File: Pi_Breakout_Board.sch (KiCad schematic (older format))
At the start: 74 parts, among them J1 Raspberry_Pi_2_3, J2 Conn_02x04_Odd_Even heater he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, J3 Conn_02x08_Odd_Even thermisto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, J4 Screw_Terminal_01x02, J5 Conn_01x08_Male, J6 Conn_01x08_Male, J7 Conn_01x05_Male uart breakout, Q1 Q_NMOS_GDSD, Q2 Q_NMOS_GDSD, Q3 Q_NMOS_GDSD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

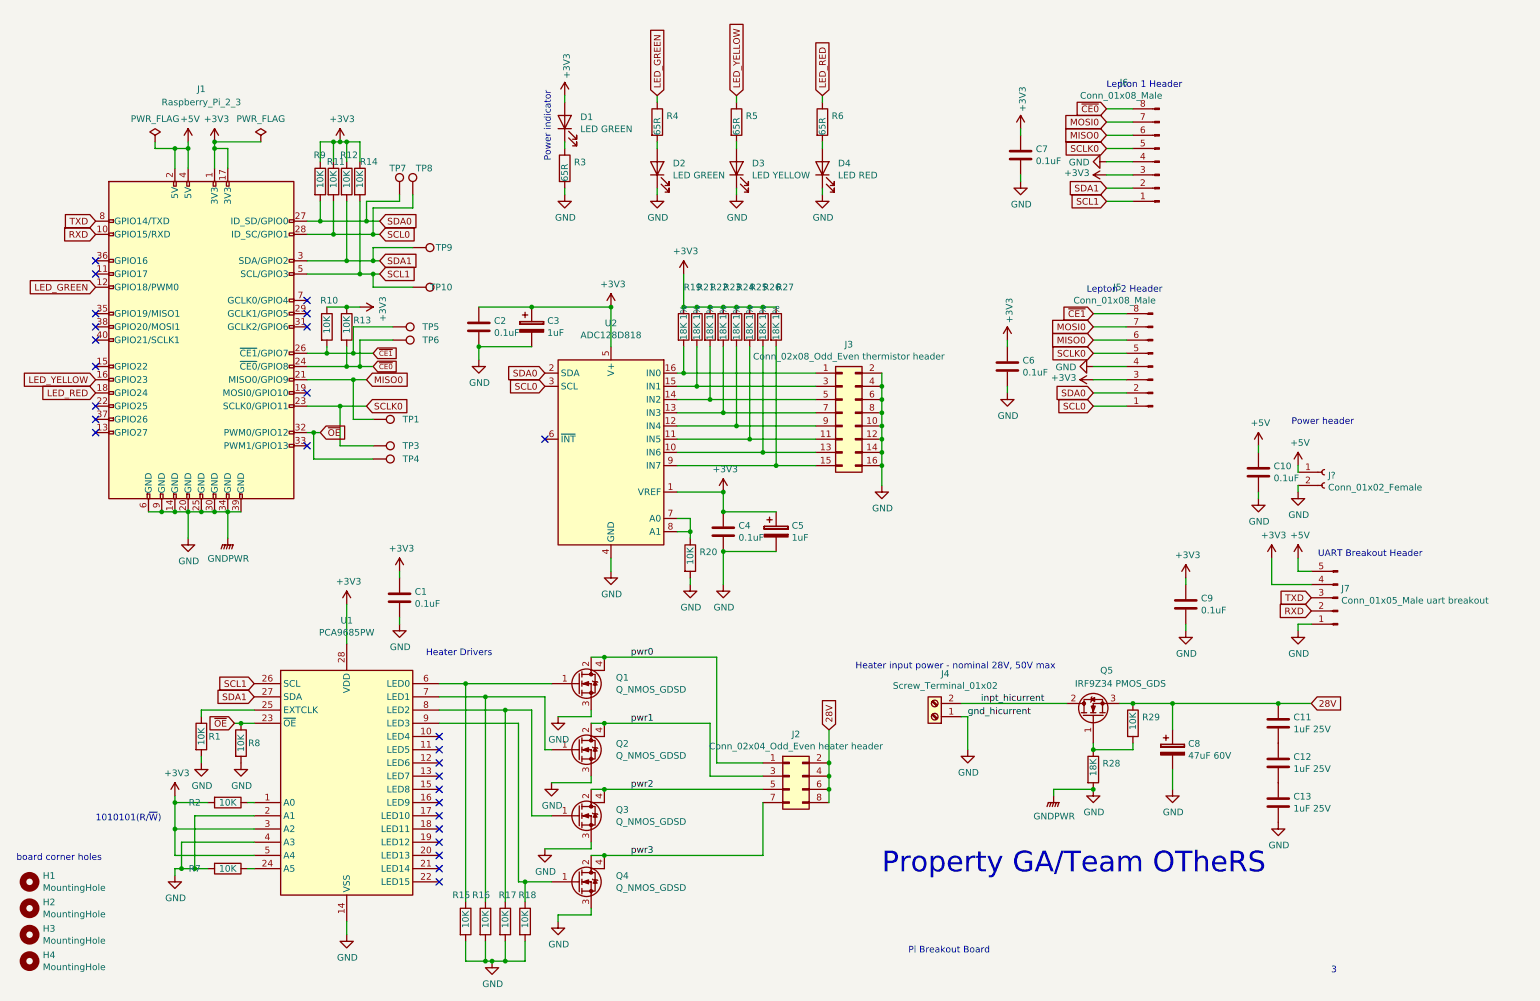
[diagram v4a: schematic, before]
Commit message: Remove power lines from UART breakout header
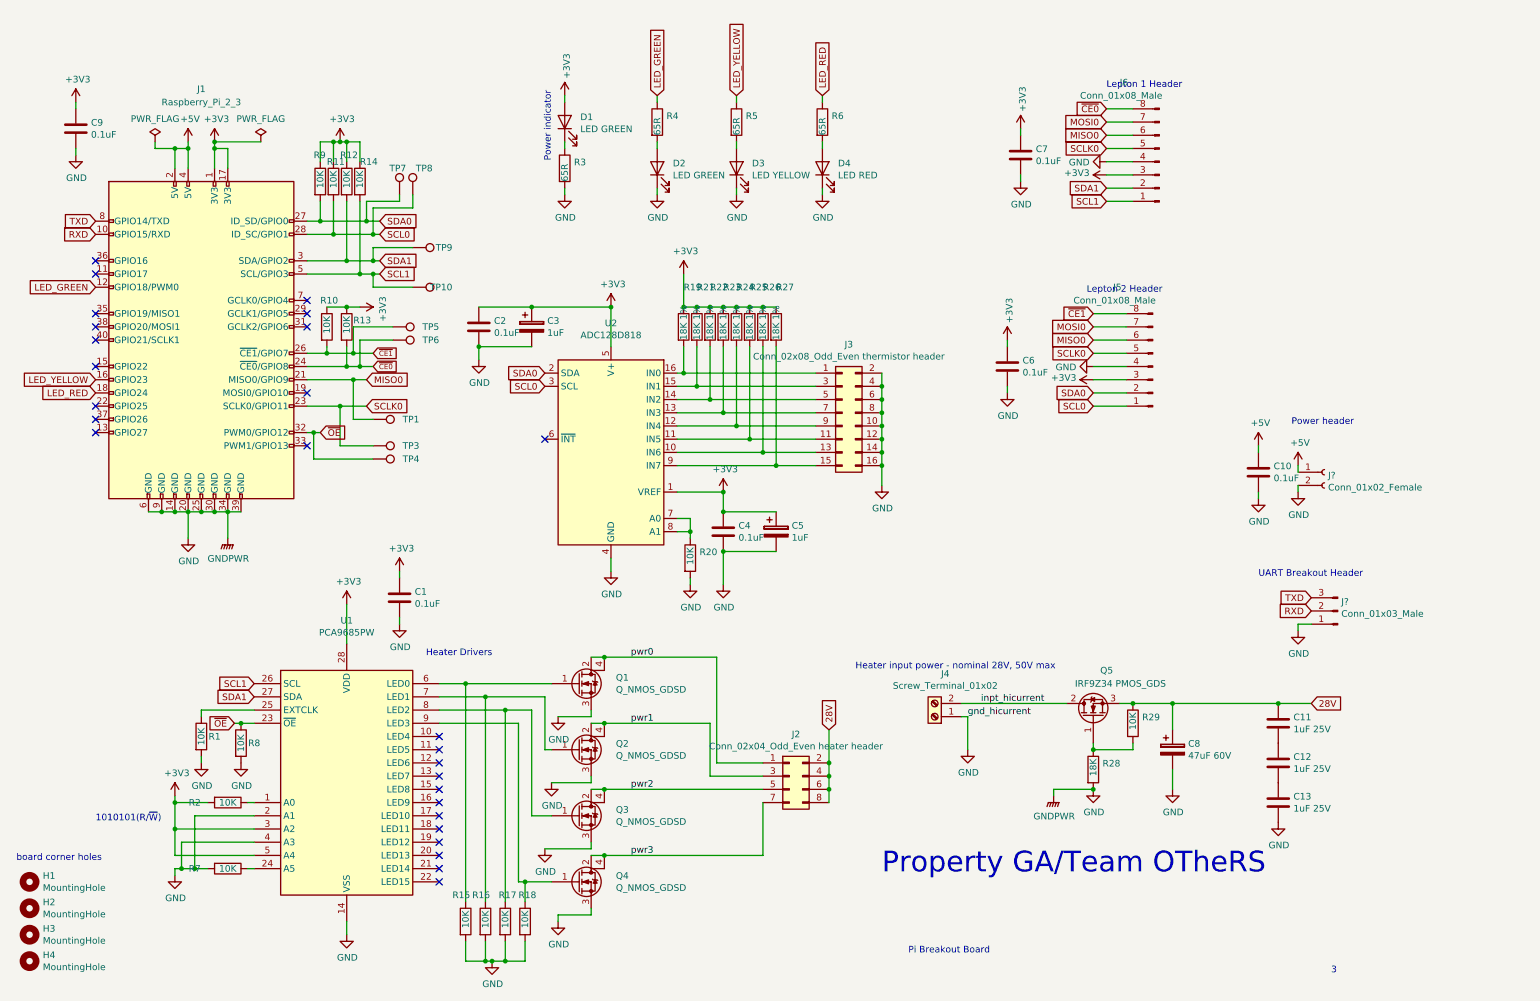
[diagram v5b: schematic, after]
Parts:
- removed J7: Conn_01x05_Male uart breakout, Connector_PinHeader_2.54mm:PinHeader_1x05_P2.54mm_Vertical, symbol Connector:Conn_01x05_Male
- added J?: Conn_01x03_Male, symbol Connector:Conn_01x03_Male
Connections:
- net GND: now also J?.1 (Pin_1)
- net RXD: now also J?.2 (Pin_2)
- net TXD: now also J?.3 (Pin_3)
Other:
- moved on the sheet: C9
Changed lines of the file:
@@
 Text GLabel 10450 4900 0    50   Input ~ 0
 RXD
-Text Notes 10500 4500 0    50   ~ 0
+Text Notes 10050 4650 0    50   ~ 0
 UART Breakout Header
 Text Notes 7000 5350 0    50   ~ 0
@@
 L Device:C C9
 U 1 1 5C58CD61
-P 9500 4850
-F 0 "C9" H 9615 4896 50  0000 L CNN
-F 1 "0.1uF" H 9615 4805 50  0000 L CNN
-F 2 "Capacitor_SMD:C_1210_3225Metric_Pad1.42x2.65mm_HandSolder" H 9538 4700 50  0001 C CNN
-F 3 "~" H 9500 4850 50  0001 C CNN
-	1    9500 4850
-	1    0    0    -1
-$EndComp
-Wire Wire Line
-	9500 4650 9500 4700
+P 1100 1250
+F 0 "C9" H 1215 1296 50  0000 L CNN
+F 1 "0.1uF" H 1215 1205 50  0000 L CNN
+F 2 "Capacitor_SMD:C_1210_3225Metric_Pad1.42x2.65mm_HandSolder" H 1138 1100 50  0001 C CNN
+F 3 "~" H 1100 1250 50  0001 C CNN
+	1    1100 1250
+	1    0    0    -1
+$EndComp
+Wire Wire Line
+	1100 1050 1100 1100
 $Comp
 L power:GND #PWR041
 U 1 1 5C58CD69
-P 9500 5050
-F 0 "#PWR041" H 9500 4800 50  0001 C CNN
-F 1 "GND" H 9505 4877 50  0000 C CNN
-F 2 "" H 9500 5050 50  0001 C CNN
-F 3 "" H 9500 5050 50  0001 C CNN
-	1    9500 5050
-	1    0    0    -1
-$EndComp
-Wire Wire Line
-	9500 5000 9500 5050
+P 1100 1450
+F 0 "#PWR041" H 1100 1200 50  0001 C CNN
+F 1 "GND" H 1105 1277 50  0000 C CNN
+F 2 "" H 1100 1450 50  0001 C CNN
+F 3 "" H 1100 1450 50  0001 C CNN
+	1    1100 1450
+	1    0    0    -1
+$EndComp
+Wire Wire Line
+	1100 1400 1100 1450
 $Comp
 L power:+3V3 #PWR040
 U 1 1 5C59BE3C
-P 9500 4650
-F 0 "#PWR040" H 9500 4500 50  0001 C CNN
-F 1 "+3V3" H 9515 4823 50  0000 C CNN
-F 2 "" H 9500 4650 50  0001 C CNN
-F 3 "" H 9500 4650 50  0001 C CNN
-	1    9500 4650
-	1    0    0    -1
-$EndComp
-$Comp
-L Connector:Conn_01x05_Male J7
-U 1 1 5C59C913
-P 10650 4800
-F 0 "J7" H 10623 4730 50  0000 R CNN
-F 1 "Conn_01x05_Male uart breakout" H 10623 4821 50  0000 R CNN
-F 2 "Connector_PinHeader_2.54mm:PinHeader_1x05_P2.54mm_Vertical" H 10650 4800 50  0001 C CNN
-F 3 "~" H 10650 4800 50  0001 C CNN
-	1    10650 4800
-	-1   0    0    1
-$EndComp
-Wire Wire Line
-	10450 4600 10350 4600
-Wire Wire Line
-	10350 4600 10350 4500
-$Comp
-L power:+3V3 #PWR044
-U 1 1 5C5BAA9F
-P 10150 4500
-F 0 "#PWR044" H 10150 4350 50  0001 C CNN
-F 1 "+3V3" H 10165 4673 50  0000 C CNN
-F 2 "" H 10150 4500 50  0001 C CNN
-F 3 "" H 10150 4500 50  0001 C CNN
-	1    10150 4500
-	1    0    0    -1
-$EndComp
-Wire Wire Line
-	10150 4500 10150 4700
-Wire Wire Line
-	10150 4700 10450 4700
+P 1100 1050
+F 0 "#PWR040" H 1100 900 50  0001 C CNN
+F 1 "+3V3" H 1115 1223 50  0000 C CNN
+F 2 "" H 1100 1050 50  0001 C CNN
+F 3 "" H 1100 1050 50  0001 C CNN
+	1    1100 1050
+	1    0    0    -1
+$EndComp
 $Comp
 L Device:R R7
@@
 Power header
 $Comp
-L power:+5V #PWR?
-U 1 1 5C94934F
-P 10350 4500
-F 0 "#PWR?" H 10350 4350 50  0001 C CNN
-F 1 "+5V" H 10365 4673 50  0000 C CNN
-F 2 "" H 10350 4500 50  0001 C CNN
-F 3 "" H 10350 4500 50  0001 C CNN
-	1    10350 4500
-	1    0    0    -1
+L Connector:Conn_01x03_Male J?
+U 1 1 5C9743D8
+P 10650 4900
+F 0 "J?" H 10623 4830 50  0000 R CNN
+F 1 "Conn_01x03_Male" H 10623 4921 50  0000 R CNN
+F 2 "" H 10650 4900 50  0001 C CNN
+F 3 "~" H 10650 4900 50  0001 C CNN
+	1    10650 4900
+	-1   0    0    1
 $EndComp
 $EndSCHEMATC

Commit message: misc routing
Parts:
- J7: renamed from J?; footprint (none) -> Connector_PinSocket_2.54mm:PinSocket_1x02_P2.54mm_Horizontal
- J8: renamed from J?; footprint (none) -> Connector_PinHeader_2.54mm:PinHeader_1x03_P2.54mm_Vertical
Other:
- note added: "Status Indicators"
- moved on the sheet: D2, D4, R4, R6
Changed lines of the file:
@@
 L Device:LED D2
 U 1 1 5C854E19
-P 5500 1550
-F 0 "D2" V 5538 1432 50  0000 R CNN
-F 1 "LED GREEN" V 5447 1432 50  0000 R CNN
-F 2 "LED_SMD:LED_0805_2012Metric_Pad1.15x1.40mm_HandSolder" H 5500 1550 50  0001 C CNN
-F 3 "~" H 5500 1550 50  0001 C CNN
-	1    5500 1550
+P 5750 1550
+F 0 "D2" V 5788 1432 50  0000 R CNN
+F 1 "LED GREEN" H 5650 1400 50  0000 R CNN
+F 2 "LED_SMD:LED_0805_2012Metric_Pad1.15x1.40mm_HandSolder" H 5750 1550 50  0001 C CNN
+F 3 "~" H 5750 1550 50  0001 C CNN
+	1    5750 1550
 	0    -1   -1   0
 $EndComp
@@
 L power:GND #PWR050
 U 1 1 5C854E2D
-P 5500 1750
-F 0 "#PWR050" H 5500 1500 50  0001 C CNN
-F 1 "GND" H 5505 1577 50  0000 C CNN
-F 2 "" H 5500 1750 50  0001 C CNN
-F 3 "" H 5500 1750 50  0001 C CNN
-	1    5500 1750
+P 5750 1750
+F 0 "#PWR050" H 5750 1500 50  0001 C CNN
+F 1 "GND" H 5755 1577 50  0000 C CNN
+F 2 "" H 5750 1750 50  0001 C CNN
+F 3 "" H 5750 1750 50  0001 C CNN
+	1    5750 1750
 	1    0    0    -1
 $EndComp
 Wire Wire Line
-	5500 1000 5500 1050
+	5750 1000 5750 1050
 Wire Wire Line
-	5500 1350 5500 1400
+	5750 1350 5750 1400
 Wire Wire Line
-	5500 1700 5500 1750
+	5750 1700 5750 1750
 $Comp
 L Device:LED D3
@@
 P 6100 1550
 F 0 "D3" V 6138 1433 50  0000 R CNN
-F 1 "LED YELLOW" V 6047 1433 50  0000 R CNN
+F 1 "LED YELLOW" H 6000 1400 50  0000 R CNN
 F 2 "LED_SMD:LED_0805_2012Metric_Pad1.15x1.40mm_HandSolder" H 6100 1550 50  0001 C CNN
 F 3 "~" H 6100 1550 50  0001 C CNN
@@
 L Device:LED D4
 U 1 1 5C87E05E
-P 6750 1550
-F 0 "D4" V 6788 1432 50  0000 R CNN
-F 1 "LED RED" V 6697 1432 50  0000 R CNN
-F 2 "LED_SMD:LED_0805_2012Metric_Pad1.15x1.40mm_HandSolder" H 6750 1550 50  0001 C CNN
-F 3 "~" H 6750 1550 50  0001 C CNN
-	1    6750 1550
+P 6450 1550
+F 0 "D4" V 6488 1432 50  0000 R CNN
+F 1 "LED RED" H 6350 1350 50  0000 R CNN
+F 2 "LED_SMD:LED_0805_2012Metric_Pad1.15x1.40mm_HandSolder" H 6450 1550 50  0001 C CNN
+F 3 "~" H 6450 1550 50  0001 C CNN
+	1    6450 1550
 	0    -1   -1   0
 $EndComp
@@
 L power:GND #PWR052
 U 1 1 5C87E072
-P 6750 1750
-F 0 "#PWR052" H 6750 1500 50  0001 C CNN
-F 1 "GND" H 6755 1577 50  0000 C CNN
-F 2 "" H 6750 1750 50  0001 C CNN
-F 3 "" H 6750 1750 50  0001 C CNN
-	1    6750 1750
+P 6450 1750
+F 0 "#PWR052" H 6450 1500 50  0001 C CNN
+F 1 "GND" H 6455 1577 50  0000 C CNN
+F 2 "" H 6450 1750 50  0001 C CNN
+F 3 "" H 6450 1750 50  0001 C CNN
+	1    6450 1750
 	1    0    0    -1
 $EndComp
 Wire Wire Line
-	6750 1000 6750 1050
+	6450 1000 6450 1050
 Wire Wire Line
-	6750 1350 6750 1400
+	6450 1350 6450 1400
 Wire Wire Line
-	6750 1700 6750 1750
-Text GLabel 5500 1000 1    50   Input ~ 0
+	6450 1700 6450 1750
+Text GLabel 5750 1000 1    50   Input ~ 0
 LED_GREEN
 Text GLabel 6100 1000 1    50   Input ~ 0
 LED_YELLOW
-Text GLabel 6750 1000 1    50   Input ~ 0
+Text GLabel 6450 1000 1    50   Input ~ 0
 LED_RED
 Text Notes 4700 1500 1    50   ~ 0
@@
 L Device:R R4
 U 1 1 5C803FD8
-P 5500 1200
-F 0 "R4" H 5570 1246 50  0000 L CNN
-F 1 "65R" V 5500 1100 50  0000 L CNN
-F 2 "Resistor_SMD:R_0805_2012Metric_Pad1.15x1.40mm_HandSolder" V 5430 1200 50  0001 C CNN
-F 3 "~" H 5500 1200 50  0001 C CNN
-	1    5500 1200
+P 5750 1200
+F 0 "R4" H 5820 1246 50  0000 L CNN
+F 1 "65R" V 5750 1100 50  0000 L CNN
+F 2 "Resistor_SMD:R_0805_2012Metric_Pad1.15x1.40mm_HandSolder" V 5680 1200 50  0001 C CNN
+F 3 "~" H 5750 1200 50  0001 C CNN
+	1    5750 1200
 	1    0    0    -1
 $EndComp
@@
 L Device:R R6
 U 1 1 5C8044FB
-P 6750 1200
-F 0 "R6" H 6820 1246 50  0000 L CNN
-F 1 "65R" V 6750 1100 50  0000 L CNN
-F 2 "Resistor_SMD:R_0805_2012Metric_Pad1.15x1.40mm_HandSolder" V 6680 1200 50  0001 C CNN
-F 3 "~" H 6750 1200 50  0001 C CNN
-	1    6750 1200
+P 6450 1200
+F 0 "R6" H 6520 1246 50  0000 L CNN
+F 1 "65R" V 6450 1100 50  0000 L CNN
+F 2 "Resistor_SMD:R_0805_2012Metric_Pad1.15x1.40mm_HandSolder" V 6380 1200 50  0001 C CNN
+F 3 "~" H 6450 1200 50  0001 C CNN
+	1    6450 1200
 	1    0    0    -1
 $EndComp
@@
 NoConn ~ 2850 3250
 $Comp
-L Connector:Conn_01x02_Female J?
+L Connector:Conn_01x02_Female J7
 U 1 1 5C91FC8D
 P 10550 3850
-F 0 "J?" H 10577 3826 50  0000 L CNN
+F 0 "J7" H 10577 3826 50  0000 L CNN
 F 1 "Conn_01x02_Female" H 10577 3735 50  0000 L CNN
-F 2 "" H 10550 3850 50  0001 C CNN
+F 2 "Connector_PinSocket_2.54mm:PinSocket_1x02_P2.54mm_Horizontal" H 10550 3850 50  0001 C CNN
 F 3 "~" H 10550 3850 50  0001 C CNN
 	1    10550 3850
@@
 	10350 3800 10350 3850
 $Comp
-L power:GND #PWR?
+L power:GND #PWR0101
 U 1 1 5C9343D0
 P 10350 4000
-F 0 "#PWR?" H 10350 3750 50  0001 C CNN
+F 0 "#PWR0101" H 10350 3750 50  0001 C CNN
 F 1 "GND" H 10355 3827 50  0000 C CNN
 F 2 "" H 10350 4000 50  0001 C CNN
@@
 Power header
 $Comp
-L Connector:Conn_01x03_Male J?
+L Connector:Conn_01x03_Male J8
 U 1 1 5C9743D8
 P 10650 4900
-F 0 "J?" H 10623 4830 50  0000 R CNN
+F 0 "J8" H 10623 4830 50  0000 R CNN
 F 1 "Conn_01x03_Male" H 10623 4921 50  0000 R CNN
-F 2 "" H 10650 4900 50  0001 C CNN
+F 2 "Connector_PinHeader_2.54mm:PinHeader_1x03_P2.54mm_Vertical" H 10650 4900 50  0001 C CNN
 F 3 "~" H 10650 4900 50  0001 C CNN
 	1    10650 4900
 	-1   0    0    1
 $EndComp
+Text Notes 5600 1600 1    50   ~ 0
+Status Indicators
 $EndSCHEMATC
